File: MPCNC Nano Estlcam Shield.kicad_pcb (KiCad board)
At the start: 2 copper layers, 160 x 100 mm, 81 parts, among them J1 Screw_Terminal_01x02, J10 Conn_01x04_Male, J11 Conn_01x04_Male, J12 Screw_Terminal_01x03, J13 Screw_Terminal_01x03, J14 Screw_Terminal_01x03, J15 Conn_02x03_Odd_Even, J16 Screw_Terminal_01x02, J17 Screw_Terminal_01x02, J18 Screw_Terminal_01x03, J19 Screw_Terminal_01x03, J2 Conn_01x03_Male, J20 Screw_Terminal_01x03, J21 Screw_Terminal_01x03, J22 Screw_Terminal_01x03, J23 Screw_Terminal_01x03, J24 Screw_Terminal_01x03, J25 Screw_Terminal_01x03, J26 Screw_Terminal_01x03, J27 Screw_Terminal_01x03, J28 Conn_01x03_Female, J3 Conn_01x06_Male, J4 Screw_Terminal_01x03, J5 Screw_Terminal_01x03, J6 Screw_Terminal_01x03, J7 Conn_01x04_Male, J8 Conn_01x04_Male, J9 Conn_01x04_Male, U1 LM358, U2 LTV-847, U3 LTV-847, U4 LTV-847, U5 ULN2003, U6 L7805, U7 ATtiny45-20PU

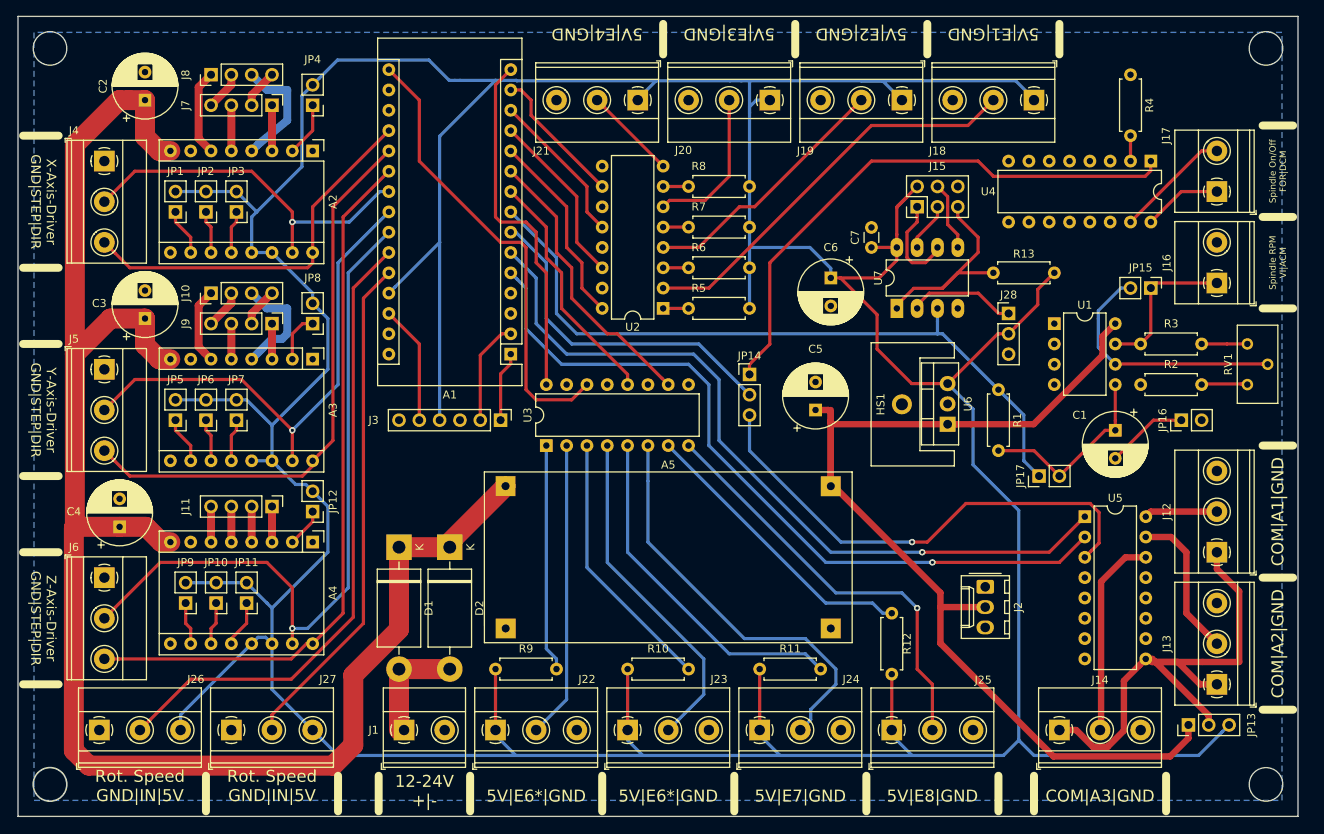
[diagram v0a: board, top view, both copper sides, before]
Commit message: V1.2
- Version 1.2 of MPCNC Nano Estlcam Shield
   PCB schematic changes:
    + Power LEDs (5mm LED) added(5V and VMot[formerly VDD])
    + 3,3V connector added
    + Output Enabled LEDs added (3 x 3mm LED + 1k resistor for OUT1,2,3), Pulls down ouput signal on startup
    # Replaced powerflag "VDD" with "VMot" (new custom symbol)
    + Added net names for Microstepping jumper
    # Signal "Analog_0_5V" now connected to "LM358 +"-Pin net (after instead of before LP-filter)
    # Replaced servo connector symbol (Conn_01x03_Female to Conn_01x03_Male)
    # Mirrored Microstepping and FLT jumper (Pin 1:5V, Pin 2:Signal)
    # Changed net names ("Ex"-> "INx", "Ax" -> "OUTx")
   PCB layout changes:
    # Silk screen text input/output description corrected ("Feedrate" and "E5")
    # Changed silk screen text language to English ("Ex"-> "INx", "Ax" -> "OUTx")
    # Moved traces and parts for schematic changes and increased margin
    # Added silk screen text for some parts (Arduino Nano, LM2596 step down module, Driver modules, Microstepping Jumper, Fan, 0-10V Adjustment Poti and LEDs)
    # Revised LM2596 module footprint
    # Replaced RV1 Trimmer/Potentiometer Footprint (Potentiometer_Bourns_3296Y_Vertical -> Potentiometer_Bourns_3296W_Vertical). Footprint (2 Pads) of Potentiometer_Bourns_3296Y_Vertical is still on PCB. -> It is possible to mount either potentiometer.
    # Changed TerminalBlocks footprint and pin pitch (5.08mm -> 5.00mm)
   Library changes:
    + Added power flag "VMot"
    # Renamed "DCDC_LM2596_Step_Down_Module" to "LM2596_Step_Down_Module"
    + Added modified footprints from KiCAD standard library for some components (Arduino Nano, Terminal blocks, Pololu driver breakout board, Bourns 3296W potentiomter, Heatsink for L7805) (added 3D models to footprint. However, 3D models are not published in repository for licensing reasons)
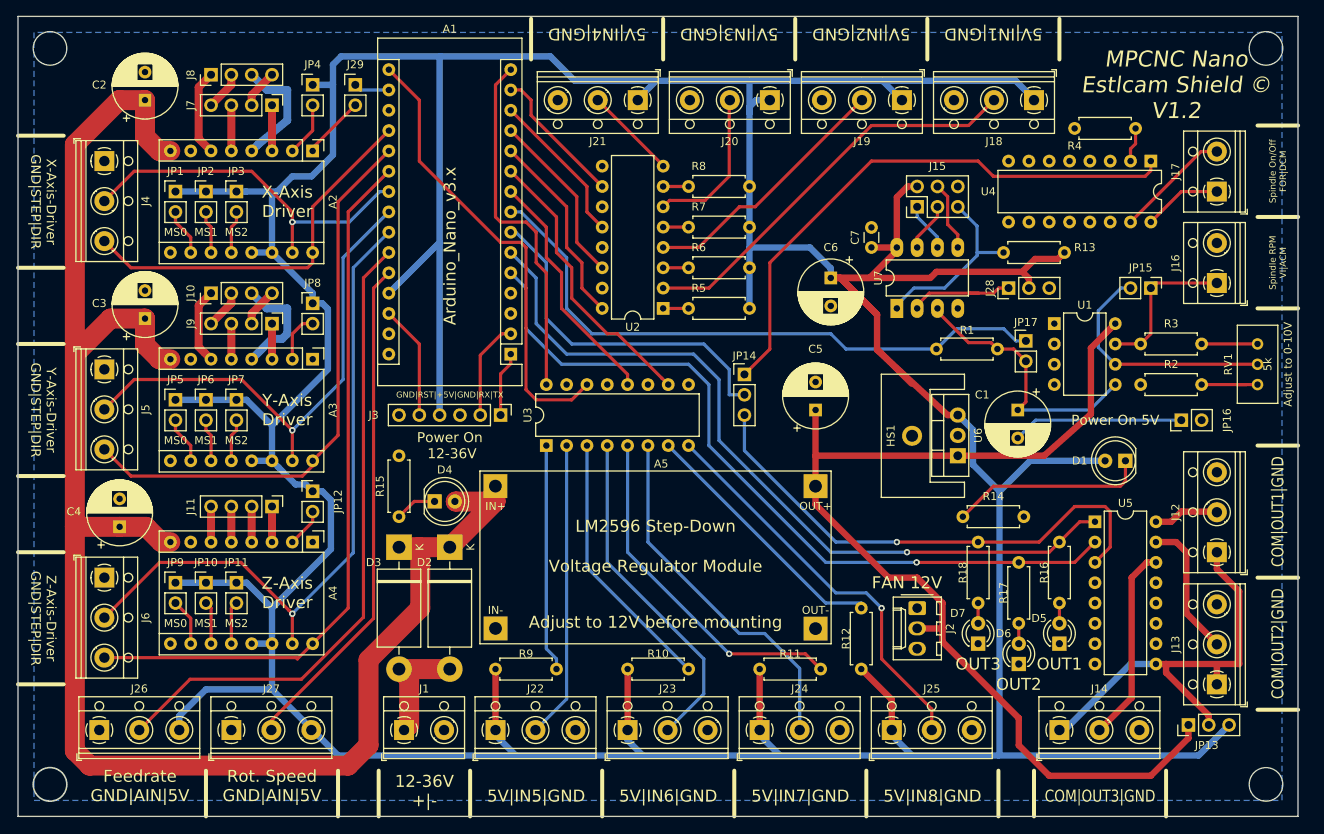
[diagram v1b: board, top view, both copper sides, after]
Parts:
- added D3: 1N5822, Diode_THT:D_DO-201AD_P15.24mm_Horizontal, F.Cu at (109.1, 107.7)
- added D4: LED RED, LED_THT:LED_D5.0mm, F.Cu at (113.6, 102.0)
- added D5: LED RED, LED_THT:LED_D3.0mm, F.Cu at (191.7, 119.8)
- added D6: LED RED, LED_THT:LED_D3.0mm, F.Cu at (186.6, 122.3)
- added D7: LED RED, LED_THT:LED_D3.0mm, F.Cu at (181.5, 119.8)
- added J29: Conn_01x02_Male, Connector_PinHeader_2.54mm:PinHeader_1x02_P2.54mm_Vertical, F.Cu at (103.7, 49.9)
- added R14: 220, Resistor_THT:R_Axial_DIN0207_L6.3mm_D2.5mm_P7.62mm_Horizontal, F.Cu at (187.2, 103.9)
- added R15: 1.8k, Resistor_THT:R_Axial_DIN0207_L6.3mm_D2.5mm_P7.62mm_Horizontal, F.Cu at (109.1, 103.9)
- added R16: 1k, Resistor_THT:R_Axial_DIN0207_L6.3mm_D2.5mm_P7.62mm_Horizontal, F.Cu at (191.7, 107.1)
- added R17: 1k, Resistor_THT:R_Axial_DIN0207_L6.3mm_D2.5mm_P7.62mm_Horizontal, F.Cu at (186.6, 109.6)
- added R18: 1k, Resistor_THT:R_Axial_DIN0207_L6.3mm_D2.5mm_P7.62mm_Horizontal, F.Cu at (181.5, 114.7)
- A1: footprint Module:Arduino_Nano -> MPCNC_Shield_Footprints:Arduino_Nano
- A2, A3, A4: footprint Module:Pololu_Breakout-16_15.2x20.3mm -> MPCNC_Shield_Footprints:Pololu_Breakout-16_15.2x20.3mm
- A5: value DCDC_LM2596_Step_Down_Module -> LM2596_Step_Down_Module; footprint Power_Module:LM2596_Module-4_21.2x40.3mm -> MPCNC_Shield_Footprints:LM2596_Step_Down_Module-21.3x43.6mm
- C6: value 0.1µF -> 1µF
- D1: value 1N5822 -> LED GREEN; footprint Diode_THT:D_DO-201AD_P15.24mm_Horizontal -> LED_THT:LED_D5.0mm
- HS1: footprint Power_Module:Heatsink_China_TO220_(22x)15x10mm_1xDrill1.5mm -> MPCNC_Shield_Footprints:Heatsink_China_TO220_(22x)15x10mm_1xDrill1.5mm
- J1, J16, J17: footprint TerminalBlock_Phoenix:TerminalBlock_Phoenix_MKDS-1,5-2-5.08_1x02_P5.08mm_Horizontal -> MPCNC_Shield_Footprints:TerminalBlock_RND_205-00012_1x02_P5.00mm_Horizontal
- J12, J13, J14, J18, J19, J20, J21, J22, J23, J24, J25, J26, J27, J4, J5, J6: footprint TerminalBlock_Phoenix:TerminalBlock_Phoenix_MKDS-1,5-3-5.08_1x03_P5.08mm_Horizontal -> MPCNC_Shield_Footprints:TerminalBlock_RND_205-00013_1x03_P5.00mm_Horizontal
- J28: value Conn_01x03_Female -> Conn_01x03_Male
- JP13, JP14: value Jumper_NC_Dual -> Jumper_3_Open
- RV1: footprint Potentiometer_THT:Potentiometer_Bourns_3296Y_Vertical -> MPCNC_Shield_Footprints:Potentiometer_Bourns_3296W_Vertical
- moved D1 91.4 mm to (199.9, 96.9), turned to 180 degrees
- moved JP17 17.0 mm to (187.5, 81.9), turned to 0 degrees
- moved C1 12.5 mm to (186.5, 90.5)
- moved R4 9.69 mm to (193.6, 55.4), turned to 0 degrees
- moved R1 9.26 mm to (176.3, 82.9), turned to 0 degrees
- moved J2 8.92 mm to (173.9, 115.3)
- moved HS1 4.14 mm to (173.3, 93.7)
- moved U6 4.14 mm to (179.0, 96.3)
- moved R12 3.86 mm to (166.9, 122.9)
- moved J28 3.17 mm to (185.3, 75.3), turned to 90 degrees
- moved JP10 2.84 mm to (85.0, 112.1), turned to 0 degrees
- moved JP11 2.84 mm to (88.8, 112.1), turned to 0 degrees
- moved JP9 2.84 mm to (81.2, 112.1), turned to 0 degrees
- moved R13 2.84 mm to (184.7, 70.9)
- moved JP12 2.54 mm to (98.3, 100.7), turned to 0 degrees
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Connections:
- net /A1 renamed /OUT1
- net /A2 renamed /OUT2
- net /A3 renamed /OUT3
- net /E1 renamed /IN1
- net /E1_R_LED renamed /IN1_R_LED
- net /E2 renamed /IN2
- net /E2_R_LED renamed /IN2_R_LED
- net /E3 renamed /IN3
- net /E3_R_LED renamed /IN3_R_LED
- net /E4 renamed /IN4
- net /E4_R_LED renamed /IN4_R_LED
- net /E5 renamed /IN5
- net /E5_R_LED renamed /IN5_R_LED
- net /E6 renamed /IN6
- net /E6_R_LED renamed /IN6_R_LED
- net /E7 renamed /IN7
- net /E7_R_LED renamed /IN7_R_LED
- net /E8 renamed /IN8
- net /E8_R_LED renamed /IN8_R_LED
- net Net-(C1-Pad2) renamed /C1_to_JP16
- net Net-(R2-Pad2) renamed /RV1_R2
- net Net-(R3-Pad1) renamed /R3_RV1
- net Net-(R4-Pad2) renamed /SPINDEL_ON_OFF_R_LED
- A1 pad 17: Net-(A1-Pad17) -> +3V3
- A1 pad 8: Analog_0-5V|PWM -> /Spindle_PWM(D5)
- A2 pad 10: Net-(A2-Pad10) -> /M0X
- A2 pad 11: Net-(A2-Pad11) -> /M1X
- A2 pad 12: Net-(A2-Pad12) -> /M2X
- A2 pad 8: VDD -> VMot
- A3 pad 10: Net-(A3-Pad10) -> /M0Y
- A3 pad 11: Net-(A3-Pad11) -> /M1Y
- A3 pad 12: Net-(A3-Pad12) -> /M2Y
- A3 pad 8: VDD -> VMot
- A4 pad 10: Net-(A4-Pad10) -> /M0Z
- A4 pad 11: Net-(A4-Pad11) -> /M1Z
- A4 pad 12: Net-(A4-Pad12) -> /M2Z
- A4 pad 8: VDD -> VMot
- A5 pad 1: VDD -> VMot
- C1 pad 1: Net-(C1-Pad1) -> Spindle_Speed_Analog_0-5V
- C2 pad 1: VDD -> VMot
- C3 pad 1: VDD -> VMot
- C4 pad 1: VDD -> VMot
- D1 pad 1: VDD -> /D1_R_LED
- D1 pad 2: +VDC -> +5V
- D2 pad 1: VDD -> VMot
- D2 pad 2: +VDC -> VDC
- J1 pad 1: +VDC -> VDC
- JP1 pad 1: Net-(A2-Pad10) -> +5V
- JP1 pad 2: +5V -> /M0X
- JP10 pad 1: Net-(A4-Pad11) -> +5V
- JP10 pad 2: +5V -> /M1Z
- JP11 pad 1: Net-(A4-Pad12) -> +5V
- JP11 pad 2: +5V -> /M2Z
- JP12 pad 1: /FLT_Z -> +5V
- JP12 pad 2: +5V -> /FLT_Z
- JP17 pad 1: Analog_0-5V|PWM -> /Spindle_PWM(D5)
- JP17 pad 2: Net-(C1-Pad1) -> Spindle_Speed_Analog_0-5V
- JP2 pad 1: Net-(A2-Pad11) -> +5V
- JP2 pad 2: +5V -> /M1X
- JP3 pad 1: Net-(A2-Pad12) -> +5V
- JP3 pad 2: +5V -> /M2X
- JP4 pad 1: /FLT_X -> +5V
- JP4 pad 2: +5V -> /FLT_X
- JP5 pad 1: Net-(A3-Pad10) -> +5V
- JP5 pad 2: +5V -> /M0Y
- JP6 pad 1: Net-(A3-Pad11) -> +5V
- JP6 pad 2: +5V -> /M1Y
- JP7 pad 1: Net-(A3-Pad12) -> +5V
- JP7 pad 2: +5V -> /M2Y
- JP8 pad 1: /FLT_Y -> +5V
- JP8 pad 2: +5V -> /FLT_Y
- JP9 pad 1: Net-(A4-Pad10) -> +5V
- JP9 pad 2: +5V -> /M0Z
- R1 pad 1: Analog_0-5V|PWM -> /Spindle_PWM(D5)
- R1 pad 2: Net-(C1-Pad1) -> Spindle_Speed_Analog_0-5V
- U1 pad 5: Net-(C1-Pad1) -> Spindle_Speed_Analog_0-5V
- U7 pad 3: Analog_0-5V|PWM -> Spindle_Speed_Analog_0-5V
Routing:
- net VMot: track 0.00 -> 212.6 mm
- net VDD: track 206.2 -> 0.00 mm
- net Analog_0-5V|PWM: track 90.3 -> 0.00 mm
- net /Spindle_PWM(D5): track 0.00 -> 76.9 mm
- net +5V: track 639.4 -> 685.5 mm
- net Spindle_Speed_Analog_0-5V: track 0.00 -> 34.0 mm
- net /D1_R_LED: track 0.00 -> 24.7 mm
- net Net-(C1-Pad1): track 24.0 -> 0.00 mm
- net VDC: track 0.00 -> 15.7 mm
- net /COM: track 67.9 -> 53.1 mm
- net +VDC: track 14.0 -> 0.00 mm
- net /C1_to_JP16: track 10.2 -> 21.4 mm
- net GND: track 0.00 -> 7.92 mm
- net /IN7: track 51.6 -> 45.3 mm
- net /M2Z: track 0.00 -> 5.98 mm
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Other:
- net class 5V: clearance 0.2 -> 0.4; trace_width 0.4 -> 0.8
- net class Power: trace_width 2.5 -> 3
- net class VDD removed
- net class VMot added: clearance 0.5, trace_width 3, via_dia 1.6, via_drill 0.8
- board text added: "12-36V +|-"
- board text added: "5V|IN1|GND"
- board text added: "5V|IN2|GND"
- board text added: "5V|IN3|GND"
- board text added: "5V|IN4|GND"
- board text added: "5V|IN5|GND"
- board text added: "5V|IN6|GND"
- board text added: "5V|IN7|GND"
- board text added: "5V|IN8|GND"
- board text added: "Adjust to 0-10V"
- board text added: "COM|OUT1|GND"
- board text added: "COM|OUT2|GND"
- board text added: "COM|OUT3|GND"
- board text added: "FAN 12V"
- board text added: "Feedrate GND|AIN|5V"
- board text added: "GND|RST|+5V|GND|RX|TX"
- board text added: "MPCNC Nano Estlcam Shield © V1.2"
- board text added: "MS0"
- board text added: "MS1"
- board text added: "MS2"
- board text added: "OUT1"
- board text added: "OUT2"
- board text added: "OUT3"
- board text added: "Power On 12-36V"
- board text added: "Power On 5V"
- board text added: "Rot. Speed GND|AIN|5V"
- board text added: "X-Axis Driver"
- board text added: "Y-Axis Driver"
- board text added: "Z-Axis Driver"
- board text removed: "12-24V +|-"
- board text removed: "5V|E1|GND"
- board text removed: "5V|E2|GND"
- board text removed: "5V|E3|GND"
- board text removed: "5V|E4|GND"
- board text removed: "5V|E6*|GND"
- board text removed: "5V|E7|GND"
- board text removed: "5V|E8|GND"
- board text removed: "COM|A1|GND"
- board text removed: "COM|A2|GND"
- board text removed: "COM|A3|GND"
- board text removed: "Rot. Speed GND|IN|5V"

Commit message: Revert "V1.2"
This reverts commit 25746ea092c74b1b8c6b498096b07c9fdffcdb93.
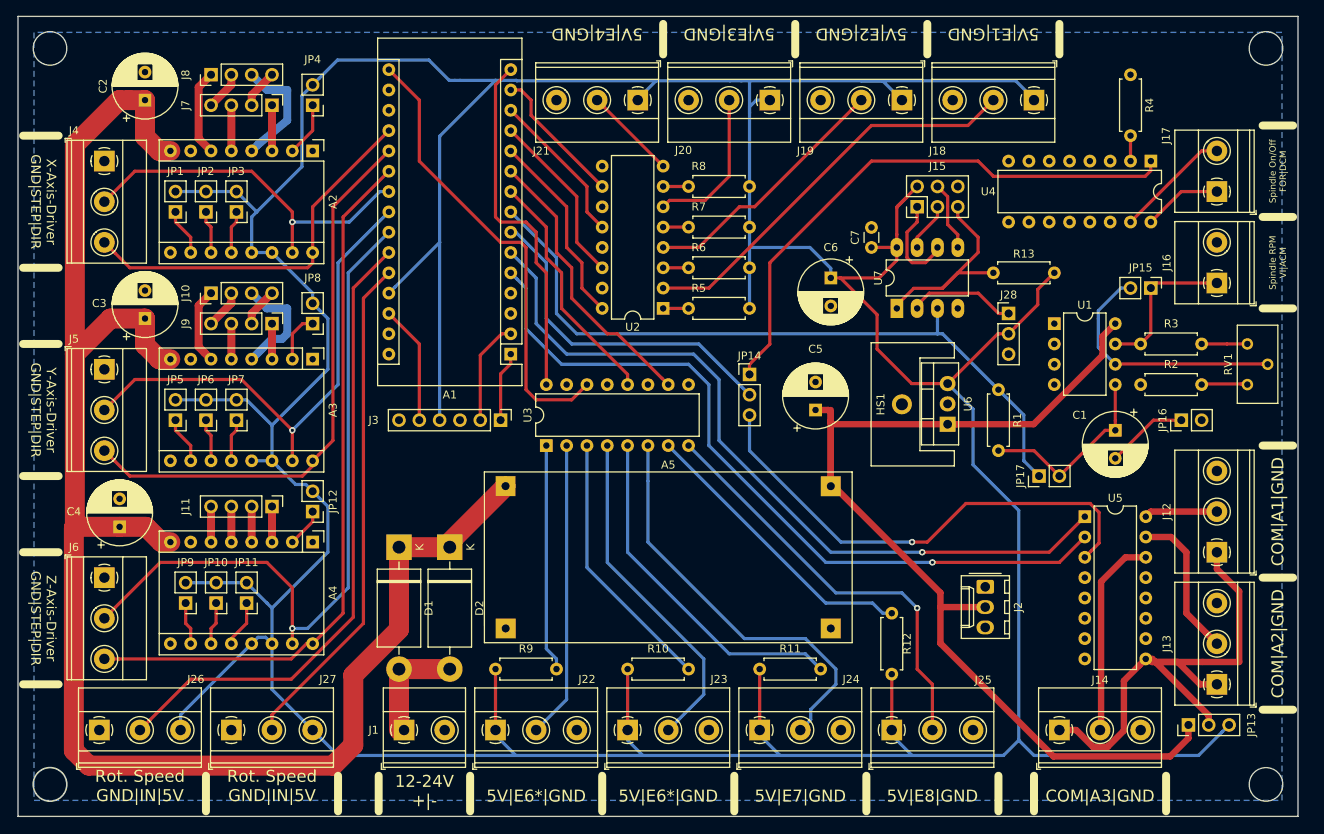
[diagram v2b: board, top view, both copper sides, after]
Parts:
- removed D3: 1N5822, Diode_THT:D_DO-201AD_P15.24mm_Horizontal
- removed D4: LED RED, LED_THT:LED_D5.0mm
- removed D5, D6, D7: LED RED, LED_THT:LED_D3.0mm
- removed J29: Conn_01x02_Male, Connector_PinHeader_2.54mm:PinHeader_1x02_P2.54mm_Vertical
- removed R14: 220, Resistor_THT:R_Axial_DIN0207_L6.3mm_D2.5mm_P7.62mm_Horizontal
- removed R15: 1.8k, Resistor_THT:R_Axial_DIN0207_L6.3mm_D2.5mm_P7.62mm_Horizontal
- removed R16, R17, R18: 1k, Resistor_THT:R_Axial_DIN0207_L6.3mm_D2.5mm_P7.62mm_Horizontal
- A1: footprint MPCNC_Shield_Footprints:Arduino_Nano -> Module:Arduino_Nano
- A2, A3, A4: footprint MPCNC_Shield_Footprints:Pololu_Breakout-16_15.2x20.3mm -> Module:Pololu_Breakout-16_15.2x20.3mm
- A5: value LM2596_Step_Down_Module -> DCDC_LM2596_Step_Down_Module; footprint MPCNC_Shield_Footprints:LM2596_Step_Down_Module-21.3x43.6mm -> Power_Module:LM2596_Module-4_21.2x40.3mm
- C6: value 1µF -> 0.1µF
- D1: value LED GREEN -> 1N5822; footprint LED_THT:LED_D5.0mm -> Diode_THT:D_DO-201AD_P15.24mm_Horizontal
- HS1: footprint MPCNC_Shield_Footprints:Heatsink_China_TO220_(22x)15x10mm_1xDrill1.5mm -> Power_Module:Heatsink_China_TO220_(22x)15x10mm_1xDrill1.5mm
- J1, J16, J17: footprint MPCNC_Shield_Footprints:TerminalBlock_RND_205-00012_1x02_P5.00mm_Horizontal -> TerminalBlock_Phoenix:TerminalBlock_Phoenix_MKDS-1,5-2-5.08_1x02_P5.08mm_Horizontal
- J12, J13, J14, J18, J19, J20, J21, J22, J23, J24, J25, J26, J27, J4, J5, J6: footprint MPCNC_Shield_Footprints:TerminalBlock_RND_205-00013_1x03_P5.00mm_Horizontal -> TerminalBlock_Phoenix:TerminalBlock_Phoenix_MKDS-1,5-3-5.08_1x03_P5.08mm_Horizontal
- J28: value Conn_01x03_Male -> Conn_01x03_Female
- JP13, JP14: value Jumper_3_Open -> Jumper_NC_Dual
- RV1: footprint MPCNC_Shield_Footprints:Potentiometer_Bourns_3296W_Vertical -> Potentiometer_THT:Potentiometer_Bourns_3296Y_Vertical
- moved D1 91.4 mm to (109.1, 107.7), turned to 270 degrees
- moved JP17 17.0 mm to (189.1, 98.8), turned to 90 degrees
- moved C1 12.5 mm to (198.7, 93.1)
- moved R4 9.69 mm to (200.6, 48.6), turned to 270 degrees
- moved R1 9.26 mm to (184.1, 88.0), turned to 270 degrees
- moved J2 8.92 mm to (182.4, 112.6)
- moved HS1 4.14 mm to (172.0, 89.8)
- moved U6 4.14 mm to (177.7, 92.3)
- moved R12 3.86 mm to (170.7, 123.6)
- moved J28 3.17 mm to (185.3, 78.5), turned to 0 degrees
- moved JP10 2.84 mm to (86.3, 114.7), turned to 180 degrees
- moved JP11 2.84 mm to (90.1, 114.7), turned to 180 degrees
- moved JP9 2.84 mm to (82.5, 114.7), turned to 180 degrees
- moved R13 2.84 mm to (183.4, 73.4)
- moved JP12 2.54 mm to (98.3, 103.2), turned to 180 degrees
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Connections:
- net /C1_to_JP16 renamed Net-(C1-Pad2)
- net /IN1 renamed /E1
- net /IN1_R_LED renamed /E1_R_LED
- net /IN2 renamed /E2
- net /IN2_R_LED renamed /E2_R_LED
- net /IN3 renamed /E3
- net /IN3_R_LED renamed /E3_R_LED
- net /IN4 renamed /E4
- net /IN4_R_LED renamed /E4_R_LED
- net /IN5 renamed /E5
- net /IN5_R_LED renamed /E5_R_LED
- net /IN6 renamed /E6
- net /IN6_R_LED renamed /E6_R_LED
- net /IN7 renamed /E7
- net /IN7_R_LED renamed /E7_R_LED
- net /IN8 renamed /E8
- net /IN8_R_LED renamed /E8_R_LED
- net /OUT1 renamed /A1
- net /OUT2 renamed /A2
- net /OUT3 renamed /A3
- net /R3_RV1 renamed Net-(R3-Pad1)
- net /RV1_R2 renamed Net-(R2-Pad2)
- net /SPINDEL_ON_OFF_R_LED renamed Net-(R4-Pad2)
- A1 pad 17: +3V3 -> Net-(A1-Pad17)
- A1 pad 8: /Spindle_PWM(D5) -> Analog_0-5V|PWM
- A2 pad 10: /M0X -> Net-(A2-Pad10)
- A2 pad 11: /M1X -> Net-(A2-Pad11)
- A2 pad 12: /M2X -> Net-(A2-Pad12)
- A2 pad 8: VMot -> VDD
- A3 pad 10: /M0Y -> Net-(A3-Pad10)
- A3 pad 11: /M1Y -> Net-(A3-Pad11)
- A3 pad 12: /M2Y -> Net-(A3-Pad12)
- A3 pad 8: VMot -> VDD
- A4 pad 10: /M0Z -> Net-(A4-Pad10)
- A4 pad 11: /M1Z -> Net-(A4-Pad11)
- A4 pad 12: /M2Z -> Net-(A4-Pad12)
- A4 pad 8: VMot -> VDD
- A5 pad 1: VMot -> VDD
- C1 pad 1: Spindle_Speed_Analog_0-5V -> Net-(C1-Pad1)
- C2 pad 1: VMot -> VDD
- C3 pad 1: VMot -> VDD
- C4 pad 1: VMot -> VDD
- D1 pad 1: /D1_R_LED -> VDD
- D1 pad 2: +5V -> +VDC
- D2 pad 1: VMot -> VDD
- D2 pad 2: VDC -> +VDC
- J1 pad 1: VDC -> +VDC
- JP1 pad 1: +5V -> Net-(A2-Pad10)
- JP1 pad 2: /M0X -> +5V
- JP10 pad 1: +5V -> Net-(A4-Pad11)
- JP10 pad 2: /M1Z -> +5V
- JP11 pad 1: +5V -> Net-(A4-Pad12)
- JP11 pad 2: /M2Z -> +5V
- JP12 pad 1: +5V -> /FLT_Z
- JP12 pad 2: /FLT_Z -> +5V
- JP17 pad 1: /Spindle_PWM(D5) -> Analog_0-5V|PWM
- JP17 pad 2: Spindle_Speed_Analog_0-5V -> Net-(C1-Pad1)
- JP2 pad 1: +5V -> Net-(A2-Pad11)
- JP2 pad 2: /M1X -> +5V
- JP3 pad 1: +5V -> Net-(A2-Pad12)
- JP3 pad 2: /M2X -> +5V
- JP4 pad 1: +5V -> /FLT_X
- JP4 pad 2: /FLT_X -> +5V
- JP5 pad 1: +5V -> Net-(A3-Pad10)
- JP5 pad 2: /M0Y -> +5V
- JP6 pad 1: +5V -> Net-(A3-Pad11)
- JP6 pad 2: /M1Y -> +5V
- JP7 pad 1: +5V -> Net-(A3-Pad12)
- JP7 pad 2: /M2Y -> +5V
- JP8 pad 1: +5V -> /FLT_Y
- JP8 pad 2: /FLT_Y -> +5V
- JP9 pad 1: +5V -> Net-(A4-Pad10)
- JP9 pad 2: /M0Z -> +5V
- R1 pad 1: /Spindle_PWM(D5) -> Analog_0-5V|PWM
- R1 pad 2: Spindle_Speed_Analog_0-5V -> Net-(C1-Pad1)
- U1 pad 5: Spindle_Speed_Analog_0-5V -> Net-(C1-Pad1)
- U7 pad 3: Spindle_Speed_Analog_0-5V -> Analog_0-5V|PWM
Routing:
- net VMot: track 212.6 -> 0.00 mm
- net VDD: track 0.00 -> 206.2 mm
- net Analog_0-5V|PWM: track 0.00 -> 90.3 mm
- net /Spindle_PWM(D5): track 76.9 -> 0.00 mm
- net +5V: track 685.5 -> 639.4 mm
- net Spindle_Speed_Analog_0-5V: track 34.0 -> 0.00 mm
- net /D1_R_LED: track 24.7 -> 0.00 mm
- net Net-(C1-Pad1): track 0.00 -> 24.0 mm
- net VDC: track 15.7 -> 0.00 mm
- net /COM: track 53.1 -> 67.9 mm
- net +VDC: track 0.00 -> 14.0 mm
- net Net-(C1-Pad2): track 21.4 -> 10.2 mm
- net GND: track 7.92 -> 0.00 mm
- net /E7: track 45.3 -> 51.6 mm
- net /M2Z: track 5.98 -> 0.00 mm
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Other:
- net class 5V: clearance 0.4 -> 0.2; trace_width 0.8 -> 0.4
- net class Power: trace_width 3 -> 2.5
- net class VDD added: clearance 0.5, trace_width 2.5, via_dia 1.6, via_drill 0.8
- net class VMot removed
- board text added: "12-24V +|-"
- board text added: "5V|E1|GND"
- board text added: "5V|E2|GND"
- board text added: "5V|E3|GND"
- board text added: "5V|E4|GND"
- board text added: "5V|E6*|GND"
- board text added: "5V|E7|GND"
- board text added: "5V|E8|GND"
- board text added: "COM|A1|GND"
- board text added: "COM|A2|GND"
- board text added: "COM|A3|GND"
- board text added: "Rot. Speed GND|IN|5V"
- board text removed: "12-36V +|-"
- board text removed: "5V|IN1|GND"
- board text removed: "5V|IN2|GND"
- board text removed: "5V|IN3|GND"
- board text removed: "5V|IN4|GND"
- board text removed: "5V|IN5|GND"
- board text removed: "5V|IN6|GND"
- board text removed: "5V|IN7|GND"
- board text removed: "5V|IN8|GND"
- board text removed: "Adjust to 0-10V"
- board text removed: "COM|OUT1|GND"
- board text removed: "COM|OUT2|GND"
- board text removed: "COM|OUT3|GND"
- board text removed: "FAN 12V"
- board text removed: "Feedrate GND|AIN|5V"
- board text removed: "GND|RST|+5V|GND|RX|TX"
- board text removed: "MPCNC Nano Estlcam Shield © V1.2"
- board text removed: "MS0"
- board text removed: "MS1"
- board text removed: "MS2"
- board text removed: "OUT1"
- board text removed: "OUT2"
- board text removed: "OUT3"
- board text removed: "Power On 12-36V"
- board text removed: "Power On 5V"
- board text removed: "Rot. Speed GND|AIN|5V"
- board text removed: "X-Axis Driver"
- board text removed: "Y-Axis Driver"
- board text removed: "Z-Axis Driver"
